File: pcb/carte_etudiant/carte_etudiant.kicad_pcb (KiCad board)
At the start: 2 copper layers, 70 x 77.5 mm, 3 parts, among them J1 Conn_02x15_Odd_Even, J2 Conn_01x14, U1 NUCLEO64-F103RB

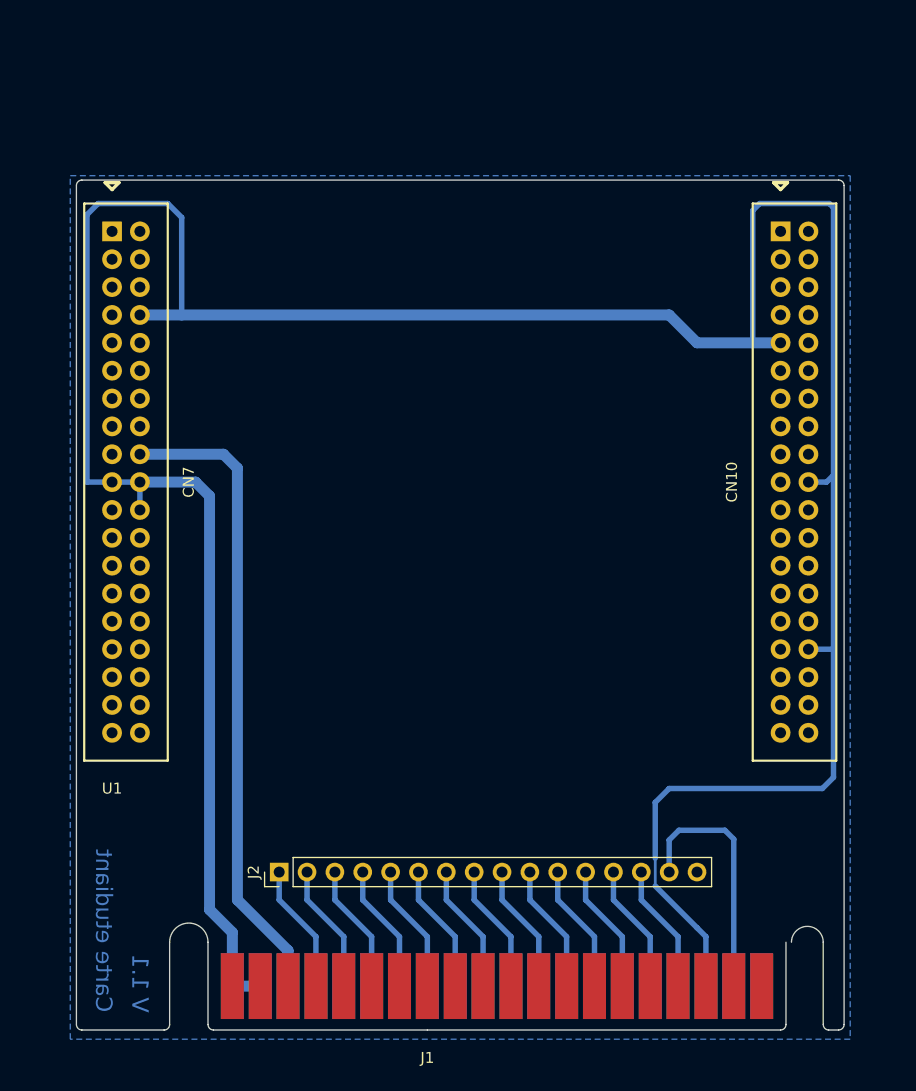
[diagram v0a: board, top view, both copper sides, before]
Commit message: modif sur la carte etudiant (changement de coté)
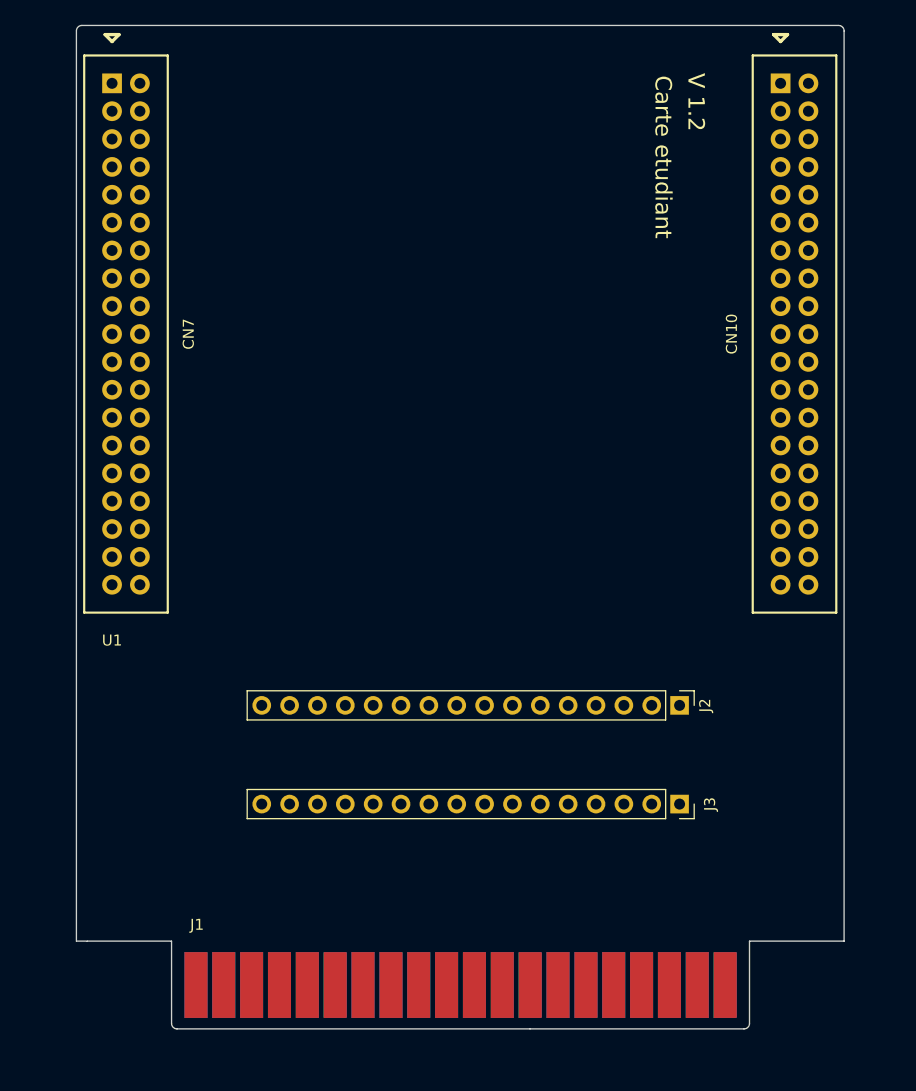
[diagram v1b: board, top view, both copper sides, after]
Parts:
- added J3: Conn_01x14, Connector_PinSocket_2.54mm:PinSocket_1x16_P2.54mm_Vertical, F.Cu at (147.0, 133.5)
- J1: moved to B.Cu
- moved J2 39.5 mm to (147.0, 124.5), turned to 270 degrees
- moved U1 13.5 mm to (127.0, 113.5)
- moved J1 9.38 mm to (133.4, 154.0), turned to 180 degrees
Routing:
- net GND: track 277.2 -> 0.00 mm
- net +5V: track 58.6 -> 0.00 mm
- net /TENSION_BATTERIE: track 22.9 -> 0.00 mm
- net /GIROUETTE_INDEX: track 11.8 -> 0.00 mm
- net /CAPTEUR_I2C_SDA: track 11.8 -> 0.00 mm
- net /SERVO_VOILE_PWM: track 11.8 -> 0.00 mm
- net /PLATEAU_PWM: track 11.8 -> 0.00 mm
- net /CAPTEUR_SPI_MOSI: track 11.8 -> 0.00 mm
- net /CAPTEUR_SPI_CLK: track 11.8 -> 0.00 mm
- net /XBEE_UART_TX: track 11.8 -> 0.00 mm
- net /XBEE_UART_RX: track 11.8 -> 0.00 mm
- net /PLATEAU_DIRECTION: track 11.8 -> 0.00 mm
- net /GIROUETTE_PHB: track 11.8 -> 0.00 mm
- net /GIROUETTE_PHA: track 11.8 -> 0.00 mm
- net /CAPTEUR_SPI_MISO: track 11.8 -> 0.00 mm
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- removed copper zone on B.Cu, net GND
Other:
- board size 70 x 77.5 mm -> 70 x 83.5 mm
- board text added: "V 1.2"
- board text removed: "V 1.1"

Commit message: carte terminée
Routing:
- net GND: track 0.00 -> 315.0 mm
- net +5V: track 0.00 -> 116.9 mm
- net /TENSION_BATTERIE: track 0.00 -> 39.2 mm
- net /XBEE_UART_TX: track 0.00 -> 28.1 mm
- net /PLATEAU_DIRECTION: track 0.00 -> 28.1 mm
- net /XBEE_UART_RX: track 0.00 -> 28.1 mm
- net /CAPTEUR_SPI_MISO: track 0.00 -> 28.1 mm
- net /PLATEAU_PWM: track 0.00 -> 28.1 mm
- net /CAPTEUR_SPI_MOSI: track 0.00 -> 28.1 mm
- net /CAPTEUR_SPI_CS: track 0.00 -> 28.1 mm
- net /CAPTEUR_I2C_SCL: track 0.00 -> 28.1 mm
- net /SERVO_VOILE_PWM: track 0.00 -> 28.1 mm
- net /CAPTEUR_I2C_SDA: track 0.00 -> 28.1 mm
- net /GIROUETTE_PHB: track 0.00 -> 28.1 mm
- net /GIROUETTE_PHA: track 0.00 -> 28.1 mm
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- added copper zone on F.Cu, net GND
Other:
- board size 70 x 83.5 mm -> 76 x 83 mm
- board text added: "Girouette A"
- board text added: "Girouette B"
- board text added: "Girouette Idx."
- board text added: "I2C SCL"
- board text added: "I2C SDA"
- board text added: "Plateau Dir."
- board text added: "Plateau PWM"
- board text added: "SPI CLK"
- board text added: "SPI CS"
- board text added: "SPI MISO"
- board text added: "SPI MOSI"
- board text added: "Servo PWM"
- board text added: "Tension Bat."
- board text added: "UART RX"
- board text added: "UART TX"

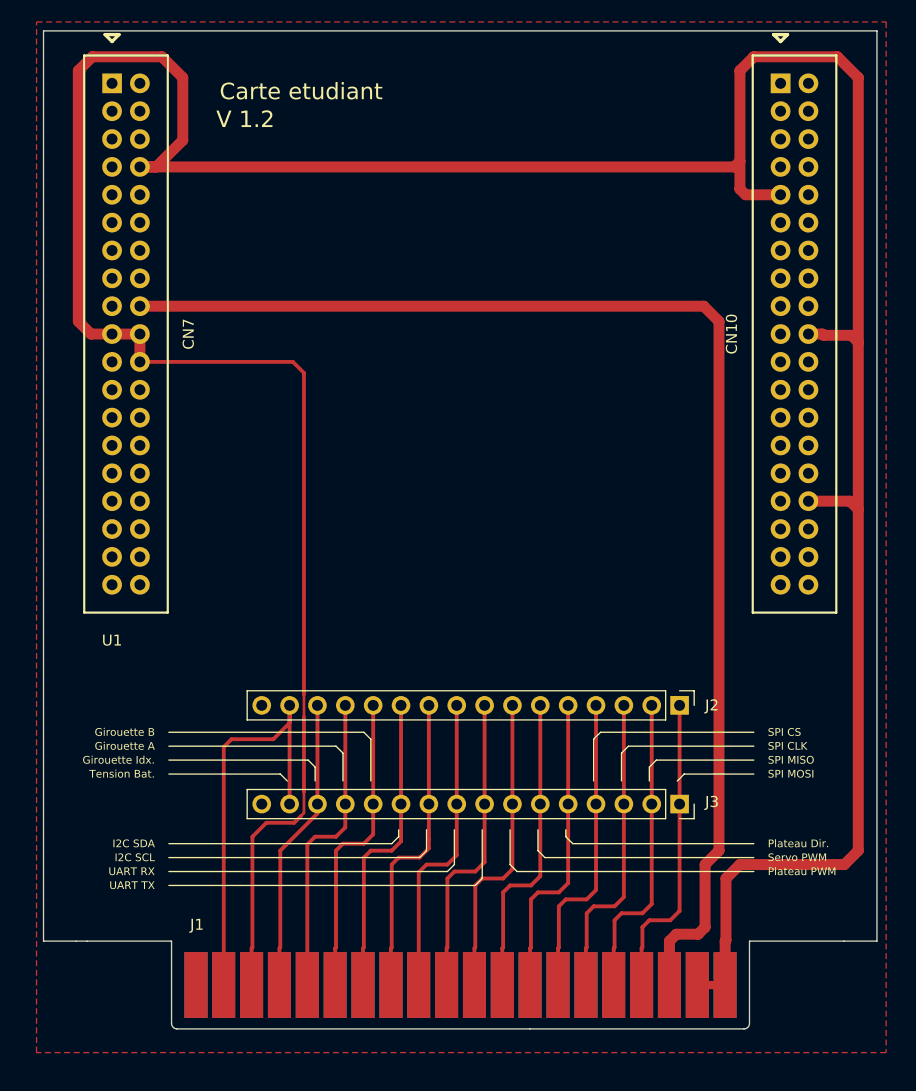
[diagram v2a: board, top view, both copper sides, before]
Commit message: retournement des connecteurs de bords de carte
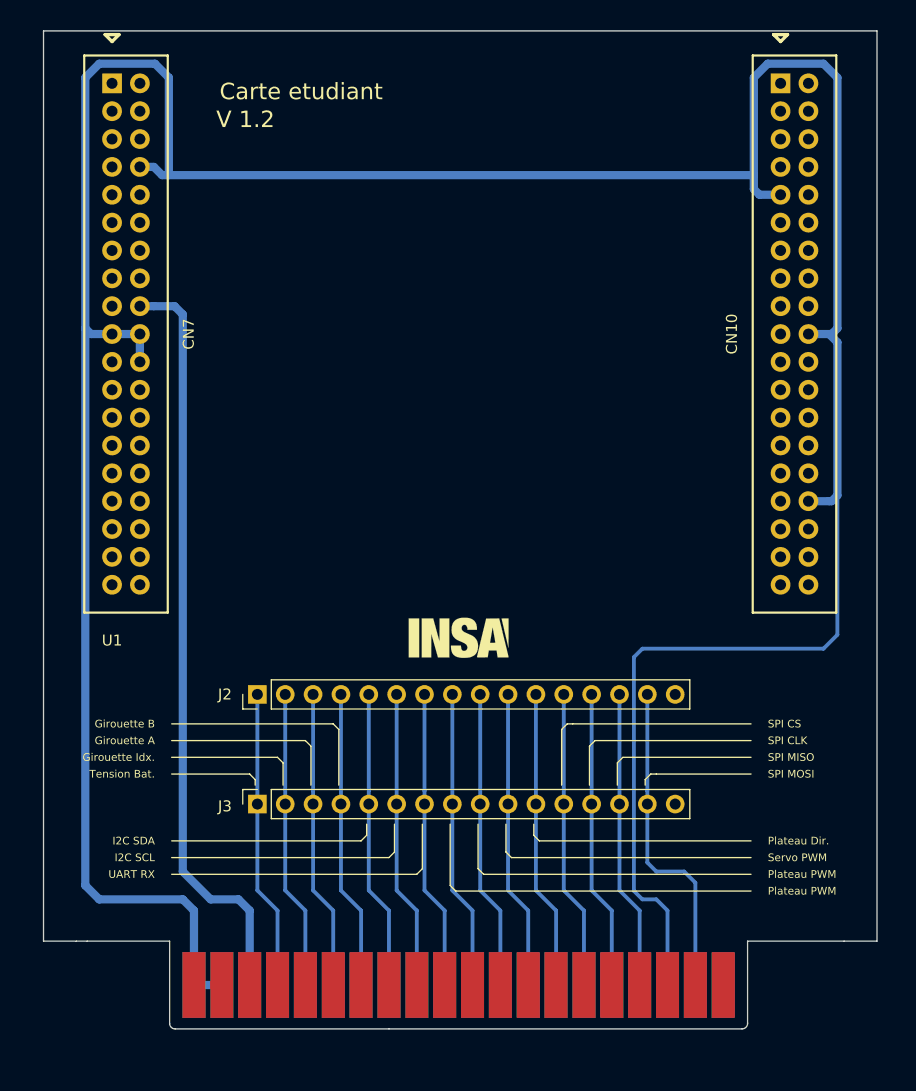
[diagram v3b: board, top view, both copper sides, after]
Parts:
- added G***: LOGO, Insa:insa-image, F.Cu at (127.0, 118.5)
- J1: moved to F.Cu
- moved J2 38.5 mm to (108.5, 123.5), turned to 90 degrees
- moved J3 38.5 mm to (108.5, 133.5), turned to 90 degrees
- moved J1 12.9 mm to (120.5, 154.0), turned to 0 degrees
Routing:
- net +5V: track 116.9 -> 69.4 mm
- net GND: track 315.0 -> 304.5 mm
- net /TENSION_BATTERIE: track 39.2 -> 29.8 mm
- net /CAPTEUR_I2C_SCL: track 28.1 -> 27.3 mm
- net /CAPTEUR_SPI_MISO: track 28.1 -> 27.3 mm
- net /CAPTEUR_SPI_CS: track 28.1 -> 27.3 mm
- net /XBEE_UART_TX: track 28.1 -> 27.3 mm
- net /PLATEAU_DIRECTION: track 28.1 -> 27.3 mm
- net /XBEE_UART_RX: track 28.1 -> 27.3 mm
- net /PLATEAU_PWM: track 28.1 -> 27.3 mm
- net /CAPTEUR_SPI_MOSI: track 28.1 -> 27.3 mm
- net /SERVO_VOILE_PWM: track 28.1 -> 27.3 mm
- net /CAPTEUR_I2C_SDA: track 28.1 -> 27.3 mm
- net /GIROUETTE_PHB: track 28.1 -> 27.3 mm
- net /GIROUETTE_PHA: track 28.1 -> 27.3 mm
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- removed copper zone on F.Cu, net GND
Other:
- outline, holes or cut-outs redrawn
- board text removed: "UART TX"

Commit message: Changement d'orientation sur carte-etudiant et pcb_acceuil
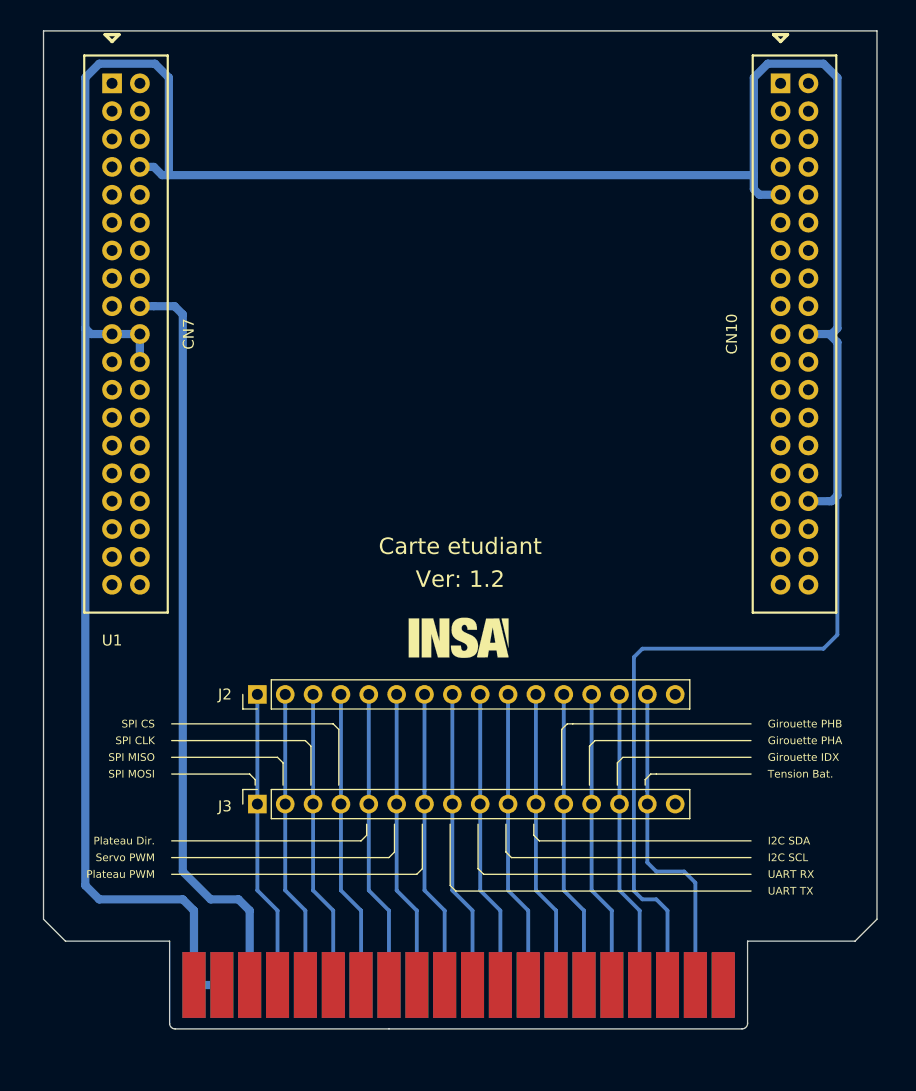
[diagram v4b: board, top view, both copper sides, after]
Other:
- outline, holes or cut-outs redrawn
- board text added: "Girouette IDX"
- board text added: "Girouette PHA"
- board text added: "Girouette PHB"
- board text added: "UART TX"
- board text added: "Ver: 1.2"
- board text removed: "Girouette A"
- board text removed: "Girouette B"
- board text removed: "Girouette Idx."
- board text removed: "V 1.2"
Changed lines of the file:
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@@
   (general
     (thickness 1.6)
-    (drawings 76)
+    (drawings 71)
     (tracks 118)
     (zones 0)
@@
   )
   (layers
-    (0 F.Cu signal)
-    (31 B.Cu jumper hide)
+    (0 F.Cu jumper)
+    (31 B.Cu signal)
+    (32 B.Adhes user)
     (33 F.Adhes user)
+    (34 B.Paste user)
     (35 F.Paste user)
+    (36 B.SilkS user)
     (37 F.SilkS user)
+    (38 B.Mask user)
     (39 F.Mask user)
     (40 Dwgs.User user)
@@
     (45 Margin user)
     (46 B.CrtYd user)
-    (47 F.CrtYd user hide)
-    (49 F.Fab user hide)
+    (47 F.CrtYd user)
   )
   (setup
-    (last_trace_width 0.35)
+    (last_trace_width 0.25)
     (user_trace_width 0.3)
     (user_trace_width 0.35)
@@
     (visible_elements FFFFFF7F)
     (pcbplotparams
-      (layerselection 0x01000_fffffffe)
+      (layerselection 0x09120_fffffffe)
       (usegerberextensions false)
       (usegerberattributes false)
@@
       (excludeedgelayer false)
       (linewidth 0.100000)
-      (plotframeref false)
+      (plotframeref true)
       (viasonmask false)
       (mode 1)
@@
     )
   )
+  (gr_line (start 91 146) (end 89 144) (layer Edge.Cuts) (width 0.12))
+  (gr_line (start 163 146) (end 165 144) (layer Edge.Cuts) (width 0.12))
   (gr_line (start 126.084 140.92) (end 126.084 135.332) (layer F.SilkS) (width 0.12))
   (gr_line (start 126.592 141.428) (end 126.084 140.92) (layer F.SilkS) (width 0.12))
@@
   (gr_line (start 134.212 136.856) (end 133.704 136.348) (layer F.SilkS) (width 0.12))
   (gr_line (start 153.516 136.856) (end 134.212 136.856) (layer F.SilkS) (width 0.12))
-  (gr_text "Plateau PWM" (at 155.04 141.428) (layer F.SilkS)
-    (effects (font (size 0.7 0.7) (thickness 0.1)) (justify left))
-  )
-  (dimension 11.43 (width 0.15) (layer F.Fab)
-    (gr_text "11,430 mm" (at 94.715 160.635) (layer F.Fab)
-      (effects (font (size 1 1) (thickness 0.15)))
-    )
-    (feature1 (pts (xy 100.43 146.635) (xy 100.43 159.921421)))
-    (feature2 (pts (xy 89 146.635) (xy 89 159.921421)))
-    (crossbar (pts (xy 89 159.335) (xy 100.43 159.335)))
-    (arrow1a (pts (xy 100.43 159.335) (xy 99.303496 159.921421)))
-    (arrow1b (pts (xy 100.43 159.335) (xy 99.303496 158.748579)))
-    (arrow2a (pts (xy 89 159.335) (xy 90.126504 159.921421)))
-    (arrow2b (pts (xy 89 159.335) (xy 90.126504 158.748579)))
-  )
-  (dimension 11.43 (width 0.15) (layer F.Fab)
-    (gr_text "11,430 mm" (at 159.485 160.635) (layer F.Fab)
-      (effects (font (size 1 1) (thickness 0.15)))
-    )
-    (feature1 (pts (xy 165.2 147.27) (xy 165.2 159.921421)))
-    (feature2 (pts (xy 153.77 147.27) (xy 153.77 159.921421)))
-    (crossbar (pts (xy 153.77 159.335) (xy 165.2 159.335)))
-    (arrow1a (pts (xy 165.2 159.335) (xy 164.073496 159.921421)))
-    (arrow1b (pts (xy 165.2 159.335) (xy 164.073496 158.748579)))
-    (arrow2a (pts (xy 153.77 159.335) (xy 154.896504 159.921421)))
-    (arrow2b (pts (xy 153.77 159.335) (xy 154.896504 158.748579)))
-  )
-  (gr_text "Plateau PWM" (at 155.04 139.904) (layer F.SilkS)
-    (effects (font (size 0.7 0.7) (thickness 0.1)) (justify left))
-  )
-  (gr_text "Servo PWM" (at 155.04 138.38) (layer F.SilkS)
-    (effects (font (size 0.7 0.7) (thickness 0.1)) (justify left))
-  )
-  (gr_text "Plateau Dir." (at 155.04 136.856) (layer F.SilkS)
-    (effects (font (size 0.7 0.7) (thickness 0.1)) (justify left))
-  )
-  (gr_text "SPI CS" (at 155.04 126.188) (layer F.SilkS)
-    (effects (font (size 0.7 0.7) (thickness 0.1)) (justify left))
-  )
-  (gr_text "SPI CLK" (at 155.04 127.712) (layer F.SilkS)
-    (effects (font (size 0.7 0.7) (thickness 0.1)) (justify left))
-  )
-  (gr_text "SPI MISO" (at 155.04 129.236) (layer F.SilkS)
-    (effects (font (size 0.7 0.7) (thickness 0.1)) (justify left))
-  )
-  (gr_text "SPI MOSI" (at 155.04 130.76) (layer F.SilkS)
-    (effects (font (size 0.7 0.7) (thickness 0.1)) (justify left))
-  )
-  (gr_text "UART RX" (at 99.16 139.904) (layer F.SilkS)
+  (gr_text "UART TX" (at 155.04 141.428) (layer F.SilkS)
+    (effects (font (size 0.7 0.7) (thickness 0.1)) (justify left))
+  )
+  (gr_text "UART RX" (at 155.04 139.904) (layer F.SilkS)
+    (effects (font (size 0.7 0.7) (thickness 0.1)) (justify left))
+  )
+  (gr_text "I2C SCL" (at 155.04 138.38) (layer F.SilkS)
+    (effects (font (size 0.7 0.7) (thickness 0.1)) (justify left))
+  )
+  (gr_text "I2C SDA\n" (at 155.04 136.856) (layer F.SilkS)
+    (effects (font (size 0.7 0.7) (thickness 0.1)) (justify left))
+  )
+  (gr_text "Girouette PHB" (at 155.04 126.188) (layer F.SilkS)
+    (effects (font (size 0.7 0.7) (thickness 0.1)) (justify left))
+  )
+  (gr_text "Girouette PHA" (at 155.04 127.712) (layer F.SilkS)
+    (effects (font (size 0.7 0.7) (thickness 0.1)) (justify left))
+  )
+  (gr_text "Girouette IDX" (at 155.04 129.236) (layer F.SilkS)
+    (effects (font (size 0.7 0.7) (thickness 0.1)) (justify left))
+  )
+  (gr_text "Tension Bat." (at 155.04 130.76) (layer F.SilkS)
+    (effects (font (size 0.7 0.7) (thickness 0.1)) (justify left))
+  )
+  (gr_text "Plateau PWM" (at 99.16 139.904) (layer F.SilkS)
     (effects (font (size 0.7 0.7) (thickness 0.1)) (justify right))
   )
-  (gr_text "I2C SCL" (at 99.16 138.38) (layer F.SilkS)
+  (gr_text "Servo PWM" (at 99.16 138.38) (layer F.SilkS)
     (effects (font (size 0.7 0.7) (thickness 0.1)) (justify right))
   )
-  (gr_text "I2C SDA" (at 99.16 136.856) (layer F.SilkS)
+  (gr_text "Plateau Dir." (at 99.16 136.856) (layer F.SilkS)
     (effects (font (size 0.7 0.7) (thickness 0.1)) (justify right))
   )
-  (gr_text "Girouette B" (at 99.16 126.188) (layer F.SilkS)
+  (gr_text "SPI CS" (at 99.16 126.188) (layer F.SilkS)
     (effects (font (size 0.7 0.7) (thickness 0.1)) (justify right))
   )
-  (gr_text "Girouette A" (at 99.16 127.712) (layer F.SilkS)
+  (gr_text "SPI CLK" (at 99.16 127.712) (layer F.SilkS)
     (effects (font (size 0.7 0.7) (thickness 0.1)) (justify right))
   )
-  (gr_text "Girouette Idx." (at 99.16 129.236) (layer F.SilkS)
+  (gr_text "SPI MISO" (at 99.16 129.236) (layer F.SilkS)
     (effects (font (size 0.7 0.7) (thickness 0.1)) (justify right))
   )
-  (gr_text "Tension Bat." (at 99.16 130.76) (layer F.SilkS)
+  (gr_text "SPI MOSI" (at 99.16 130.76) (layer F.SilkS)
     (effects (font (size 0.7 0.7) (thickness 0.1)) (justify right))
   )
   (gr_line (start 165 63) (end 89 63) (layer Edge.Cuts) (width 0.12))
-  (gr_line (start 162 146) (end 165 146) (layer Edge.Cuts) (width 0.12))
-  (gr_line (start 92 146) (end 89 146) (layer Edge.Cuts) (width 0.12))
-  (gr_line (start 165 146) (end 165 63) (layer Edge.Cuts) (width 0.12))
-  (gr_line (start 89 146) (end 89 63) (layer Edge.Cuts) (width 0.12))
-  (dimension 91.5 (width 0.15) (layer F.Fab)
-    (gr_text "91,500 mm" (at 171.8 108.25 270) (layer F.Fab)
-      (effects (font (size 1 1) (thickness 0.15)))
-    )
-    (feature1 (pts (xy 161 154) (xy 171.086421 154)))
-    (feature2 (pts (xy 161 62.5) (xy 171.086421 62.5)))
-    (crossbar (pts (xy 170.5 62.5) (xy 170.5 154)))
-    (arrow1a (pts (xy 170.5 154) (xy 169.913579 152.873496)))
-    (arrow1b (pts (xy 170.5 154) (xy 171.086421 152.873496)))
-    (arrow2a (pts (xy 170.5 62.5) (xy 169.913579 63.626504)))
-    (arrow2b (pts (xy 170.5 62.5) (xy 171.086421 63.626504)))
-  )
-  (gr_line (start 93 146) (end 92 146) (layer Edge.Cuts) (width 0.12))
-  (gr_line (start 153.201 146) (end 162 146) (layer Edge.Cuts) (width 0.12))
-  (gr_line (start 100.5 146) (end 93 146) (layer Edge.Cuts) (width 0.12))
-  (gr_text "V 1.2" (at 107.415 71.07) (layer F.SilkS)
+  (gr_line (start 165 144) (end 165 63) (layer Edge.Cuts) (width 0.12))
+  (gr_line (start 89 144) (end 89 63) (layer Edge.Cuts) (width 0.12))
+  (gr_line (start 153.201 146) (end 163 146) (layer Edge.Cuts) (width 0.12))
+  (gr_line (start 100.5 146) (end 91 146) (layer Edge.Cuts) (width 0.12))
+  (gr_text "Ver: 1.2" (at 127 113) (layer F.SilkS)
     (effects (font (size 1.5 1.5) (thickness 0.3)))
   )
-  (gr_text "Carte etudiant" (at 112.495 68.53) (layer F.SilkS)
+  (gr_text "Carte etudiant" (at 127 110) (layer F.SilkS)
     (effects (font (size 1.5 1.5) (thickness 0.3)))
   )
-  (dimension 70 (width 0.15) (layer F.Fab)
-    (gr_text "70.000 mm" (at 127 53.2) (layer F.Fab)
-      (effects (font (size 1 1) (thickness 0.15)))
-    )
-    (feature1 (pts (xy 162 61.5) (xy 162 53.913579)))
-    (feature2 (pts (xy 92 61.5) (xy 92 53.913579)))
-    (crossbar (pts (xy 92 54.5) (xy 162 54.5)))
-    (arrow1a (pts (xy 162 54.5) (xy 160.873496 55.086421)))
-    (arrow1b (pts (xy 162 54.5) (xy 160.873496 53.913579)))
-    (arrow2a (pts (xy 92 54.5) (xy 93.126504 55.086421)))
-    (arrow2b (pts (xy 92 54.5) (xy 93.126504 53.913579)))
-  )
   (segment (start 160.64 105.88) (end 158.75 105.88) (width 0.75) (layer B.Cu) (net 1))
